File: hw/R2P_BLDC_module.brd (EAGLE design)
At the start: 40 x 60 mm, 59 parts, among them Q1 OPTIMOS, Q2 OPTIMOS, Q3 OPTIMOS, Q4 OPTIMOS, Q5 OPTIMOS, Q6 OPTIMOS, U1 STM32F103CX, U5 LD3985XX, X1 MICROMATCH-4

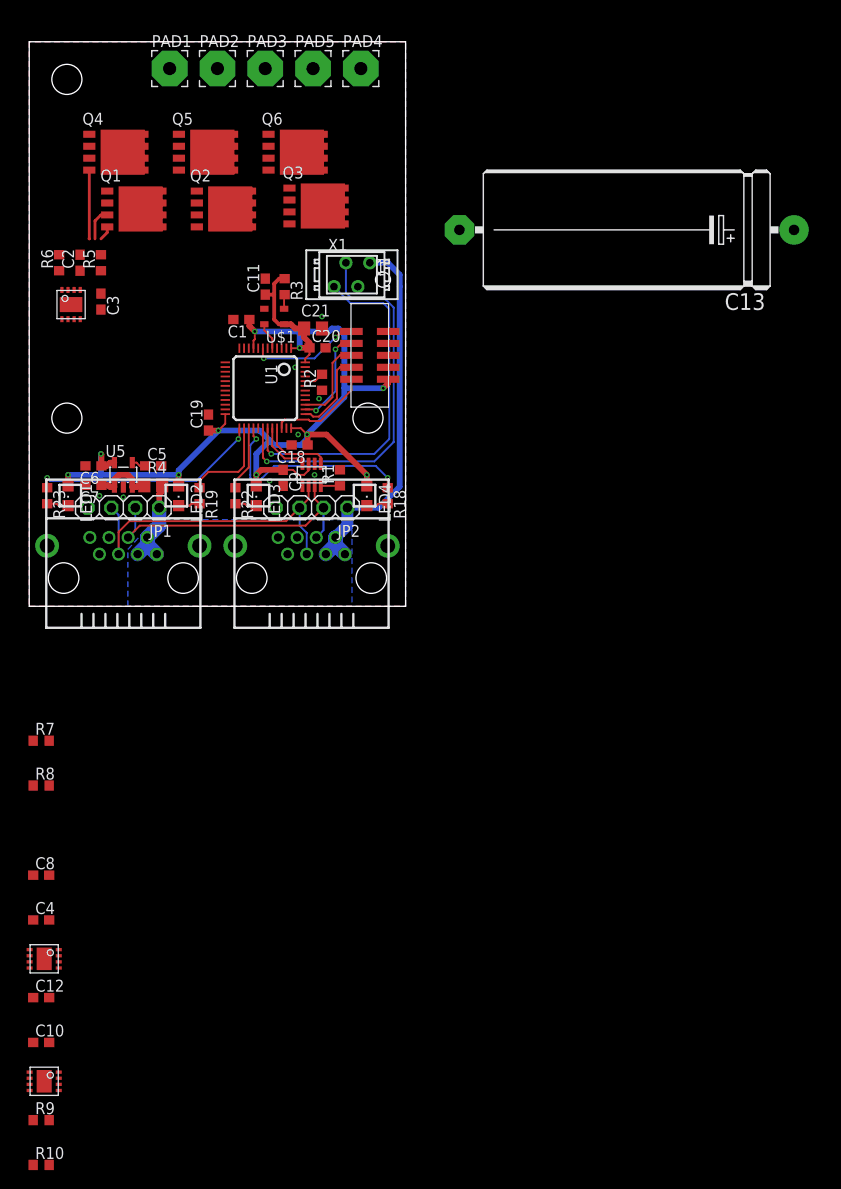
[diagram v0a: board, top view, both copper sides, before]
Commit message: H-bridge layout almost done
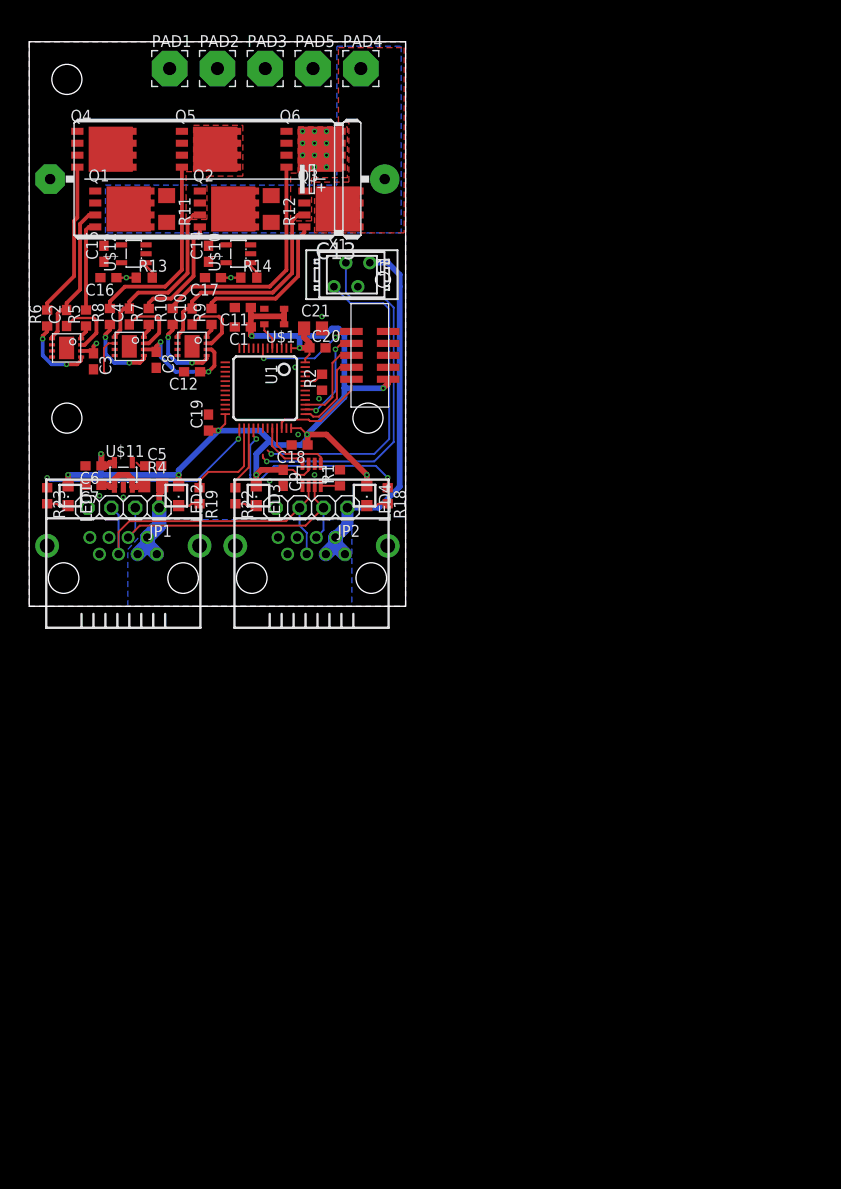
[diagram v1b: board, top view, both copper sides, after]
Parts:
- removed R3: 100k, rcl:R0603
- removed U5: LD3985XX, st:SOT23-5L
- added C14, C15, C16, C17: 100n, rcl:C0603
- added R11, R12: (no value), rcl:R1206
- added R13, R14: 10, rcl:R0603
- added U$10, U$12: INA193DBV, texas-instruments:SOT23-5L
- added U$11: TPS73033, texas-instruments:SOT23-5L
- moved R10 91.2 mm to (15.2, 30.8), turned to 90 degrees
- moved R9 87.3 mm to (19.4, 30.8), turned to 90 degrees
- moved U$9 79.7 mm to (17.3, 27.6)
- moved C10 78.8 mm to (17.3, 30.8), turned to 90 degrees
- moved C12 68.4 mm to (17.3, 24.9), turned to 180 degrees
- moved U$8 65.7 mm to (10.6, 27.6)
- moved C4 64.8 mm to (10.6, 30.8), turned to 90 degrees
- moved C8 56.1 mm to (13.5, 26.2), turned to 270 degrees
- moved R8 50.4 mm to (8.57, 30.8), turned to 90 degrees
- moved R7 46.5 mm to (12.7, 30.8), turned to 90 degrees
- moved C13 43.8 mm to (20.0, 45.4)
- moved C3 6.40 mm to (6.83, 26.0)
- moved R5 6.08 mm to (6.03, 30.6)
- moved C2 6.05 mm to (3.97, 30.6)
- moved R6 6.01 mm to (1.91, 30.6)
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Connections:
- net PWMAH renamed AH
- net PWMAL renamed AL
- removed net N$3: R3.2, U$1.1
- removed net PWMBH: U$8.P$2
- removed net PWMBL: U$8.P$3
- removed net PWMCH: U$9.P$2
- removed net PWMCL: U$9.P$3
- new net +A3V3: C14.1, C15.1, U$10.5, U$12.5, U1.9
- new net BH: U$8.P$2, U1.30
- new net BL: U$8.P$3, U1.18
- new net CH: U$9.P$2, U1.31
- new net CL: U$9.P$3, U1.19
- new net IA: C16.1, R13.1
- new net IB: C17.1, R14.1
- new net N$14: Q1.5, Q1.6, Q1.7, Q1.8, Q1.TH, R11.1, U$12.4
- new net N$16: Q2.5, Q2.6, Q2.7, Q2.8, Q2.TH, R12.1, U$10.4
- new net N$17: R13.2, U$12.1
- new net N$19: R14.2, U$10.1
- net +3V3: now also U$1.1, U$11.5; no longer R3.1, U1.9, U5.5
- net +5V: now also U$11.1, U$11.3; no longer U5.1, U5.3
- net +V: now also Q3.TH, R11.2, R12.2, U$10.3, U$12.3; no longer Q1.5, Q1.6, Q1.7, Q1.8, Q2.5, Q2.6, Q2.7, Q2.8
- net GND: now also C14.2, C15.2, C16.2, C17.2, U$10.2, U$11.2, U$12.2; no longer U5.2
- net MA: now also Q4.TH
- net MB: now also Q5.TH
- net MC: now also Q6.TH
- net N$4: now also U$11.4; no longer U5.4
- net UART_RX: now also U1.43; no longer U1.31
- net UART_TX: now also U1.42; no longer U1.30
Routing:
- net N$13: track 0.00 -> 24.9 mm
- net MC: track 0.00 -> 23.8 mm
- net N$11: track 0.00 -> 20.7 mm
- net MB: track 0.00 -> 19.3 mm
- net +5V: track 6.75 -> 23.5 mm, vias 0 -> 3
- net N$12: track 0.00 -> 16.5 mm
- net MA: track 3.47 -> 15.8 mm
- net N$9: track 0.00 -> 12.0 mm
- net N$8: track 7.33 -> 16.5 mm
- net GCL: track 0.00 -> 8.31 mm, vias 0 -> 2
- net GBL: track 0.00 -> 8.31 mm, vias 0 -> 2
- net GAL: track 0.00 -> 8.31 mm, vias 0 -> 2
- net N$7: track 1.55 -> 9.63 mm
- net N$10: track 0.00 -> 7.18 mm
- net N$5: track 0.00 -> 7.17 mm
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- added copper zone on layer 1, net +V
- added copper zone on layer 16, net +V
- added copper zone on layer 1, net MB
- added copper zone on layer 1, net MC

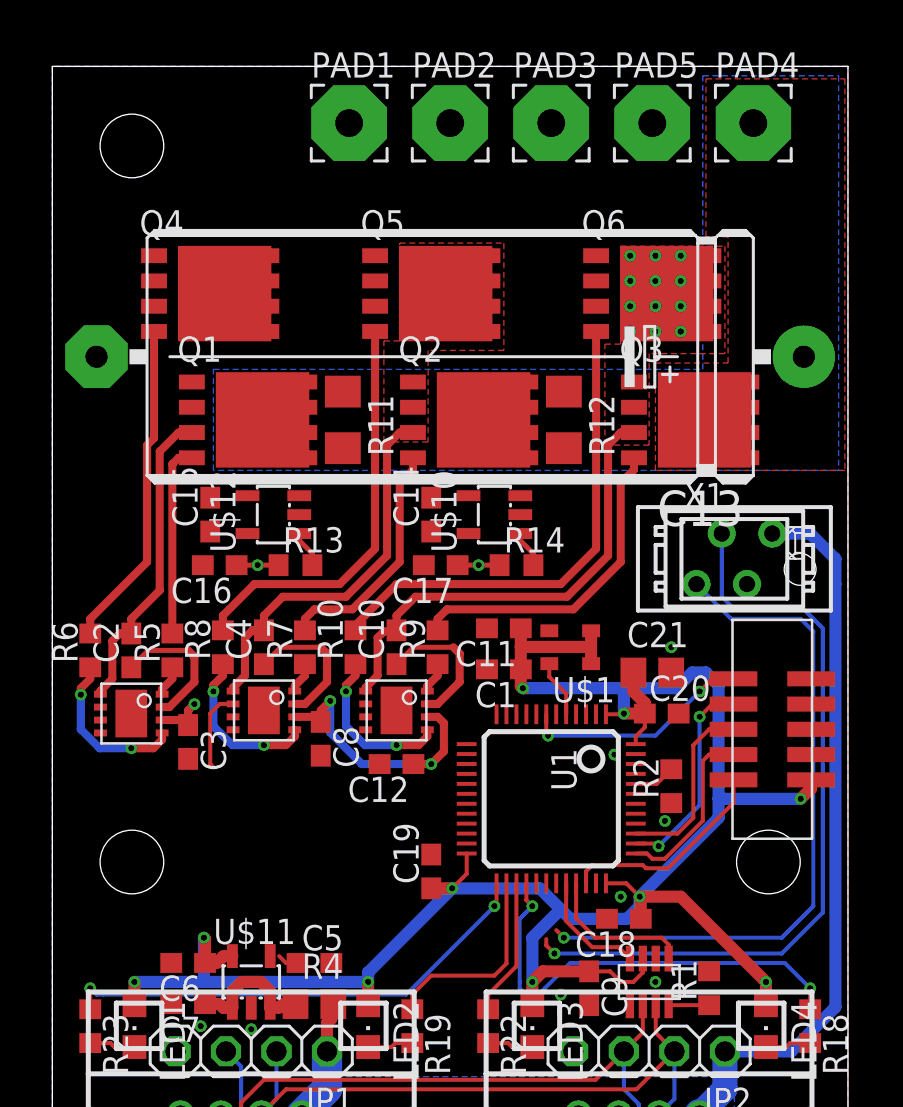
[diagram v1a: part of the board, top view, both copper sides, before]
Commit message: H-bridge layout complete
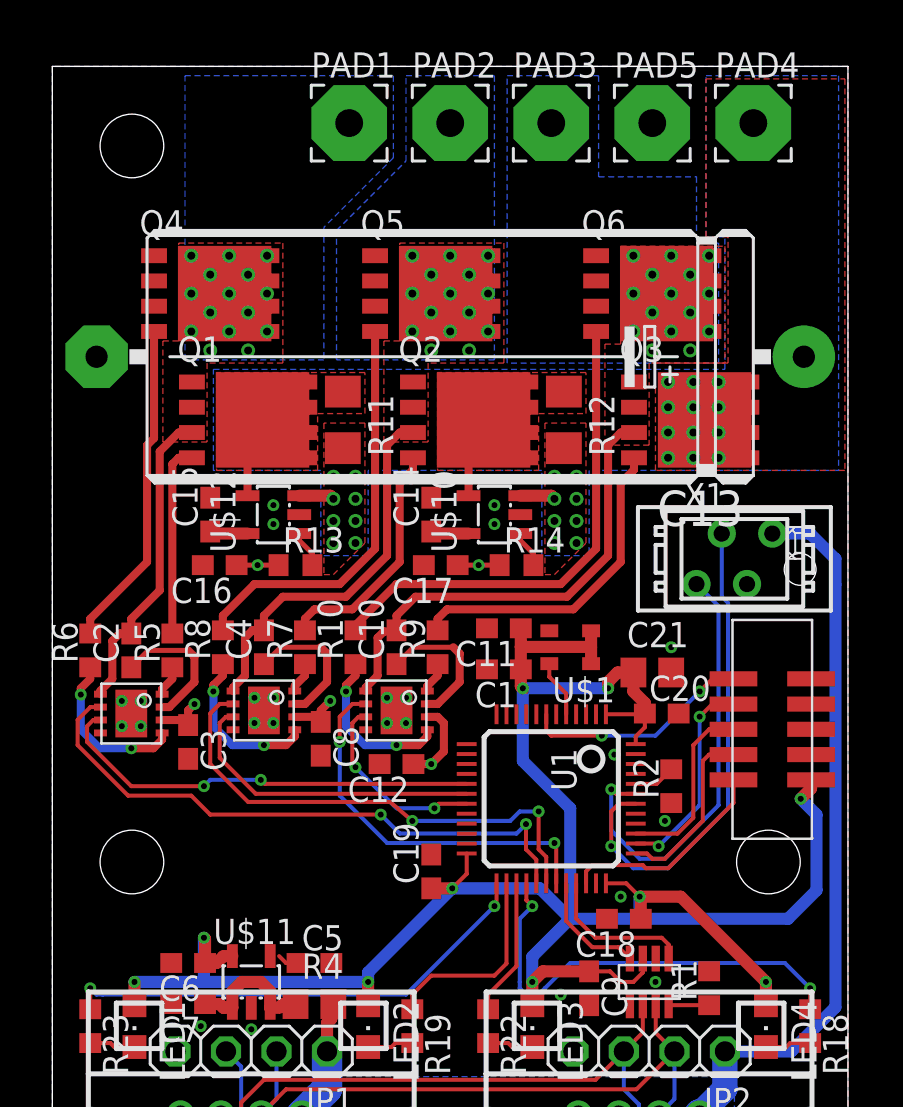
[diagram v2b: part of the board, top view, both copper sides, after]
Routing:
- net AH: track 0.00 -> 30.5 mm, vias 0 -> 2
- net AL: track 0.00 -> 21.8 mm, vias 0 -> 2
- net BH: track 4.11 -> 25.5 mm, vias 0 -> 2
- net CH: track 0.00 -> 19.4 mm, vias 0 -> 2
- net BL: track 0.00 -> 15.7 mm
- net UART_TX: track 38.4 -> 24.7 mm
- net UART_RX: track 34.4 -> 22.1 mm
- net CL: track 0.00 -> 9.63 mm, vias 0 -> 2
- net +5V: track 23.5 -> 16.2 mm
- net +3V3: track 108.1 -> 113.1 mm
- net +A3V3: track 0.00 -> 3.83 mm
- net +V: track 0.00 -> 3.56 mm, vias 0 -> 28
- net N$16: track 0.00 -> 1.99 mm
- net N$14: track 0.00 -> 1.60 mm
- net MC: vias 0 -> 15
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- added copper zone on layer 1, net MA
- added copper zone on layer 16, net MA
- added copper zone on layer 16, net MB
- added copper zone on layer 16, net MC
- added copper zone on layer 1, net N$14
- added copper zone on layer 1, net N$16

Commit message: started layout
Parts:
- removed C15, C16, C17: 100n, rcl:C0603
- removed R12: (no value), rcl:R1206
- removed R14: 10, rcl:R0603
- removed U$10, U$12: INA193DBV, texas-instruments:SOT23-5L
- removed U$8, U$9: MCP14700MF, microchip:DFN8
- added R3: 10k, rcl:R0603
- C10, C2, C4: value 15pF -> 100n
- C12: value 470nF -> 220n
- C3, C8: value 470nF -> 100n
- R11: value (none) -> 10k; device rcl:R1206 -> rcl:R0603
- R13: value 10 -> (none); device rcl:R0603 -> rcl:R2512
- U$2: value MCP14700MF -> A3930; device microchip:DFN8 -> allegro:TQFP48
- moved C14 82.3 mm to (1.11, -42.9), turned to 0 degrees
- moved R11 76.8 mm to (1.11, -33.3), turned to 0 degrees
- moved C12 65.1 mm to (1.11, -38.1), turned to 0 degrees
- moved C10 61.5 mm to (1.11, -28.6), turned to 0 degrees
- moved C8 46.9 mm to (1.11, -19.1), turned to 0 degrees
- moved C4 46.1 mm to (1.11, -14.3), turned to 0 degrees
- moved R13 24.2 mm to (28.1, 53.2), turned to 180 degrees
- moved C3 7.95 mm to (10.3, 33.2), turned to 180 degrees
- moved U$2 6.13 mm to (10.0, 26.4)
- moved R10 5.08 mm to (15.2, 35.9)
- moved R5 5.08 mm to (6.03, 35.7)
- moved R6 5.08 mm to (1.91, 35.7)
- moved R7 5.08 mm to (12.7, 35.9)
- moved R8 5.08 mm to (8.57, 35.9)
- moved C2 3.13 mm to (2.70, 27.8)
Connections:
- removed net GAH: R5.1, U$2.P$8
- removed net GAL: R6.1, U$2.P$5
- removed net GBH: R7.1, U$8.P$8
- removed net GBL: R8.1, U$8.P$5
- removed net GCH: R9.1, U$9.P$8
- removed net GCL: R10.1, U$9.P$5
- removed net IA: C16.1, R13.1
- removed net IB: C17.1, R14.1
- new net CSP: Q4.1, Q4.2, Q4.3, Q5.1, Q5.2, Q5.3, Q6.1, Q6.2, Q6.3, R13.2, U$2.22, U$2.38
- new net GHA: R5.1, U$2.32
- new net GHB: R7.1, U$2.29
- new net GHC: R9.1, U$2.26
- new net GLA: R6.1, U$2.36
- new net GLB: R8.1, U$2.35
- new net GLC: R10.1, U$2.34
- new net N$21: C12.2, U$2.3, U$2.4
- new net N$23: C14.2, U$2.40
- new net N$26: U$2.10
- new net N$27: U$2.11
- new net N$28: U$2.12
- new net N$3: C3.2, U$2.33
- net +5V: no longer C12.1, C3.1, C8.1, U$2.P$6, U$8.P$6, U$9.P$6
- net +A3V3: no longer C14.1, C15.1, U$10.5, U$12.5
- net +V: now also Q1.5, Q1.6, Q1.7, Q1.8, Q1.TH, Q2.5, Q2.6, Q2.7, Q2.8, Q2.TH, U$2.24, U$2.45; no longer R11.2, R12.2, U$10.3, U$12.3
- net AH: no longer U$2.P$2
- net AL: no longer U$2.P$3
- net BH: no longer U$8.P$2
- net BL: no longer U$8.P$3
- net CH: no longer U$9.P$2
- net CL: no longer U$9.P$3
- net GND: now also C10.2, C12.1, C14.1, R11.1, R13.1, R3.1, U$2.17, U$2.21, U$2.41, U$2.P$1; no longer C12.2, C14.2, C15.2, C16.2, C17.2, C3.2, C8.2, Q4.1, Q4.2, Q4.3, Q5.1, Q5.2, Q5.3, Q6.1, Q6.2, Q6.3, U$10.2, U$12.2, U$2.P$4, U$2.P$9, U$8.P$4, U$8.P$9, U$9.P$4, U$9.P$9
- net MA: now also C3.1, U$2.31; no longer C2.2, U$2.P$1
- net MB: now also C4.1, U$2.28; no longer C4.2, U$8.P$1
- net MC: now also C8.1, U$2.25; no longer C10.2, U$9.P$1
- net N$10: now also C2.1, U$2.43; no longer C10.1, U$9.P$7
- net N$14: now also C4.2, U$2.30; no longer Q1.5, Q1.6, Q1.7, Q1.8, Q1.TH, R11.1, U$12.4
- net N$16: now also U$2.20; no longer Q2.5, Q2.6, Q2.7, Q2.8, Q2.TH, R12.1, U$10.4
- net N$17: now also C10.1, R3.2, U$2.16; no longer R13.2, U$12.1
- net N$19: now also C8.2, U$2.27; no longer R14.2, U$10.1
- net N$5: now also C2.2, U$2.42; no longer C4.1, U$8.P$7
- net N$6: now also R11.2, U$2.18; no longer C2.1, U$2.P$7
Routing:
- net AH: track 30.5 -> 0.00 mm, vias 2 -> 0
- net BH: track 25.5 -> 0.00 mm, vias 2 -> 0
- net N$13: track 24.9 -> 0.26 mm
- net MC: track 23.8 -> 1.57 mm
- net AL: track 21.8 -> 0.00 mm, vias 2 -> 0
- net CH: track 19.4 -> 0.00 mm, vias 2 -> 0
- net BL: track 15.7 -> 0.00 mm
- net N$12: track 16.5 -> 1.55 mm
- net MB: track 19.3 -> 9.48 mm
- net MA: track 15.8 -> 5.94 mm
- net CL: track 9.63 -> 0.00 mm, vias 2 -> 0
- net N$9: track 12.0 -> 2.58 mm
- net +5V: track 16.2 -> 6.75 mm, vias 3 -> 0
- net GCL: track 8.31 -> 0.00 mm, vias 2 -> 0
- net GBL: track 8.31 -> 0.00 mm, vias 2 -> 0
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- removed copper zone on layer 1, net N$14
- removed copper zone on layer 1, net N$16

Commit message: working on layout
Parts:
- added Q7: (no value), dp_devices:SOT-23
- added R16, R17: 2.7k, rcl:R0603
- added RN1: (no value), dp_devices:RN8P-4R-CRA06S
- added X2: MICROMATCH-4, apbteam_con-amp-micromatch:MICROMATCH-4
- C11: value 15pF -> 10n
- X1: value MICROMATCH-4 -> MICROMATCH-6; device tyco:MICROMATCH-4 -> apbteam_con-amp-micromatch:MICROMATCH-6
- moved C14 72.4 mm to (2.70, 29.5)
- moved R11 62.1 mm to (17.8, 26.5), turned to 270 degrees
- moved C12 57.8 mm to (13.3, 18.4), turned to 180 degrees
- moved C8 52.9 mm to (16.0, 31.8), turned to 90 degrees
- moved C10 51.1 mm to (17.5, 19.8), turned to 90 degrees
- moved R3 49.7 mm to (17.8, 23.0), turned to 90 degrees
- moved C4 48.1 mm to (12.7, 32.4), turned to 180 degrees
- moved Q3 44.9 mm to (77.0, 43.7)
- moved Q4 44.9 mm to (52.9, 50.0)
- moved Q6 44.9 mm to (75.1, 50.0)
- moved C13 44.9 mm to (64.9, 46.8)
- moved Q1 44.9 mm to (54.8, 43.7)
- moved Q2 44.9 mm to (65.9, 43.7)
- moved Q5 44.9 mm to (64.0, 50.0)
- moved R13 23.1 mm to (50.5, 58.7), turned to 270 degrees
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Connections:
- removed net N$21 (its old number): C12.2, U$2.3, U$2.4
- removed net N$26: U$2.10
- removed net N$27: U$2.11
- removed net N$28: U$2.12
- removed net UART_RX: U1.43, X1.4
- removed net UART_TX: U1.42, X1.3
- new net ENC_A: R16.1, X2.2
- new net ENC_B: R17.1, X2.4
- new net HA: RN1.1, U$2.10, X1.3
- new net HB: RN1.2, U$2.11, X1.4
- new net HC: RN1.3, U$2.12, X1.5
- new net N$24: Q7.1, U$2.3
- new net TEMP: X1.2
- new net VHALL: C12.2, Q7.3, RN1.6, RN1.7, RN1.8, U$2.4, X1.1
- net +3V3: no longer U$1.1
- net +5V: now also R16.2, R17.2, X2.3
- net +V: now also Q7.2
- net +VBUS: no longer X1.1
- net GND: now also RN1.4, RN1.5, X1.6, X2.1; no longer X1.2
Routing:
- net UART_TX: track 24.7 -> 0.00 mm, vias 1 -> 0
- net UART_RX: track 22.1 -> 0.00 mm, vias 1 -> 0
- net N$11: track 15.6 -> 0.00 mm
- net N$8: track 11.4 -> 0.00 mm
- net MB: track 9.48 -> 0.00 mm, vias 15 -> 11
- net +5V: track 6.75 -> 13.3 mm
- net MA: track 5.94 -> 0.00 mm, vias 15 -> 11
- net N$7: track 4.55 -> 0.00 mm
- net +3V3: track 113.1 -> 108.9 mm, vias 10 -> 9
- net +VBUS: track 51.4 -> 47.9 mm
- net ENC_A: track 0.00 -> 3.02 mm
- net ENC_B: track 0.00 -> 3.02 mm
- net OSC_IN: track 2.90 -> 0.00 mm
- net N$9: track 2.58 -> 0.00 mm
- net MC: track 1.57 -> 0.00 mm, vias 15 -> 12
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- removed copper zone on layer 1, net +V
- removed copper zone on layer 16, net +V
- removed copper zone on layer 1, net MA
- removed copper zone on layer 16, net MA
- removed copper zone on layer 1, net MB
- removed copper zone on layer 16, net MB
- removed copper zone on layer 1, net MC
- removed copper zone on layer 16, net MC

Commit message: working on layout
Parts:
- moved C3 0.32 mm to (9.68, 32.7)
- moved C4 0.32 mm to (12.7, 32.7)
- moved R10 0.32 mm to (8.10, 35.2)
- moved R5 0.32 mm to (10.2, 35.2)
- moved R6 0.32 mm to (3.97, 35.2)
- moved R7 0.32 mm to (12.2, 35.2)
- moved R8 0.32 mm to (6.03, 35.2)
- moved R9 0.32 mm to (14.3, 35.2)
- turned C8 to 270 degrees
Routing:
- net GLC: track 0.00 -> 5.14 mm
- net GHC: track 0.00 -> 4.90 mm
- net GHB: track 0.00 -> 4.65 mm
- net GHA: track 0.00 -> 4.59 mm
- net MB: track 0.00 -> 2.91 mm
- net N$3: track 0.00 -> 2.84 mm
- net N$14: track 0.00 -> 2.62 mm
- net MA: track 0.00 -> 2.55 mm
- net N$19: track 0.00 -> 2.25 mm
- net GLB: track 0.00 -> 1.27 mm

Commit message: working on layout
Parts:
- removed C1: 100n, rcl:C0603
- moved R13 48.5 mm to (2.70, 50.3), turned to 90 degrees
- moved C13 45.0 mm to (20.0, 44.6)
- moved Q6 44.8 mm to (30.3, 47.6)
- moved Q3 44.8 mm to (32.2, 41.6)
- moved Q5 44.5 mm to (19.5, 47.6)
- moved Q2 44.5 mm to (21.4, 41.6)
- moved Q4 44.2 mm to (8.73, 47.6)
- moved Q1 44.2 mm to (10.6, 41.6)
- moved PAD5 20.3 mm to (9.84, 57.1)
- moved PAD4 5.08 mm to (30.2, 57.1)
- moved C14 1.42 mm to (3.33, 28.3)
- moved RN1 1.06 mm to (20.3, 30.2)
- moved C2 1.00 mm to (3.33, 26.2)
- moved C8 0.50 mm to (16.2, 31.3), turned to 0 degrees
- moved R16 0.48 mm to (35.2, 31.4)
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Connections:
- net +3V3: no longer C1.1
- net +5V: no longer R16.2, R17.2, X2.3
- net GND: no longer C1.2
- net VHALL: now also R16.2, R17.2, X2.3
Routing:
- net N$13: track 0.00 -> 28.4 mm, vias 0 -> 2
- net VHALL: track 0.00 -> 26.3 mm
- net MC: track 0.00 -> 23.7 mm, vias 12 -> 14
- net CSP: track 0.00 -> 22.7 mm
- net N$11: track 0.00 -> 19.5 mm, vias 0 -> 2
- net N$12: track 0.00 -> 17.0 mm
- net MA: track 2.55 -> 14.2 mm, vias 11 -> 14
- net N$8: track 0.00 -> 10.5 mm
- net MB: track 2.91 -> 13.1 mm, vias 11 -> 14
- net N$9: track 0.00 -> 8.56 mm
- net GLA: track 0.00 -> 6.75 mm
- net HA: track 0.00 -> 6.59 mm
- net +5V: track 13.3 -> 6.75 mm
- net HC: track 0.00 -> 5.87 mm
- net N$10: track 0.00 -> 5.27 mm
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- added copper zone on layer 1, net +V
- added copper zone on layer 16, net +V
- added copper zone on layer 1, net CSP
- added copper zone on layer 1, net MA
- added copper zone on layer 16, net MA
- added copper zone on layer 1, net MB
- added copper zone on layer 16, net MB
- added copper zone on layer 1, net MC
- added copper zone on layer 16, net MC
